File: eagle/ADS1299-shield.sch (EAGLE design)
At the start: 133 parts, among them IC1 ADS1299IPAG, IC2 TPS72325DBVT, IC3 TPS73225DBVT, IC5 24AA256UID, IC6 TPS604XXDBV, IC7 OPA376DBV, IC8 OPA376DBV, IC9 TXS0102DCTR, J16 EXTERNAL_SYNC, J8 Electrode Connector, U2 TXB0108PWR, U3 TXB0108PWR

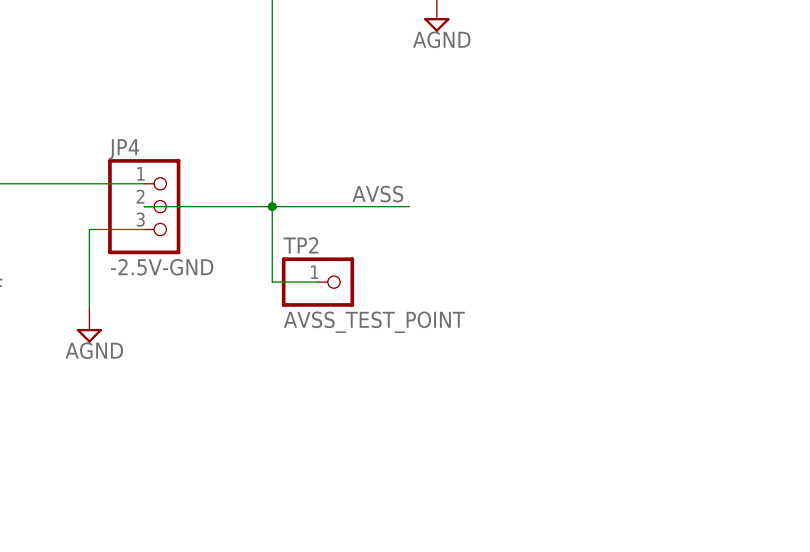
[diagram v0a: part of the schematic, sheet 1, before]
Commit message: fixed problem with test point 2
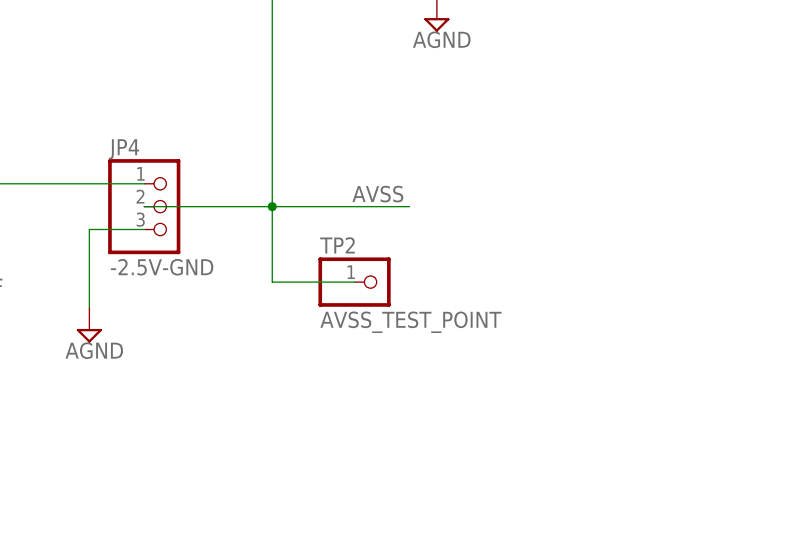
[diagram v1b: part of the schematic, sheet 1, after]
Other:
- moved on the sheet: TP2
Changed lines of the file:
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@@
 <part name="SPI" library="SmartPrj" deviceset="PINHD-2X3" device="" value="SPI"/>
 <part name="TP1" library="adafruit" deviceset="PINHD-1X1" device="" value="AVDD_TEST_POINT"/>
-<part name="TP2" library="adafruit" deviceset="PINHD-1X1" device="" value="AVSS_TEST_POINT"/>
 <part name="U$5" library="adafruit" deviceset="FIDUCIAL" device=""/>
 <part name="U$6" library="adafruit" deviceset="FIDUCIAL" device=""/>
@@
 <part name="TP3" library="adafruit" deviceset="PINHD-1X1" device="" value="AGND_TEST_POINT"/>
 <part name="SUPPLY55" library="supply2" deviceset="AGND" device=""/>
+<part name="TP2" library="adafruit" deviceset="PINHD-1X1" device="" value="AVSS_TEST_POINT"/>
 </parts>
 <sheets>
@@
 <instance part="D1" gate="G$1" x="272.034" y="43.18" rot="R90"/>
 <instance part="TP1" gate="G$1" x="184.912" y="113.792"/>
-<instance part="TP2" gate="G$1" x="184.15" y="33.782"/>
 <instance part="TP3" gate="G$1" x="212.852" y="73.152"/>
 <instance part="SUPPLY55" gate="G$1" x="194.818" y="62.992"/>
+<instance part="TP2" gate="G$1" x="188.214" y="33.782"/>
 </instances>
 <busses>
@@
 <pinref part="JP4" gate="A" pin="2"/>
 <wire x1="162.306" y1="42.164" x2="176.53" y2="42.164" width="0.1524" layer="91"/>
+<wire x1="185.674" y1="33.782" x2="176.53" y2="33.782" width="0.1524" layer="91"/>
+<wire x1="176.53" y1="33.782" x2="176.53" y2="42.164" width="0.1524" layer="91"/>
 <pinref part="TP2" gate="G$1" pin="1"/>
-<wire x1="181.61" y1="33.782" x2="176.53" y2="33.782" width="0.1524" layer="91"/>
-<wire x1="176.53" y1="33.782" x2="176.53" y2="42.164" width="0.1524" layer="91"/>
-</segment>
-<segment>
+</segment>
+<segment>

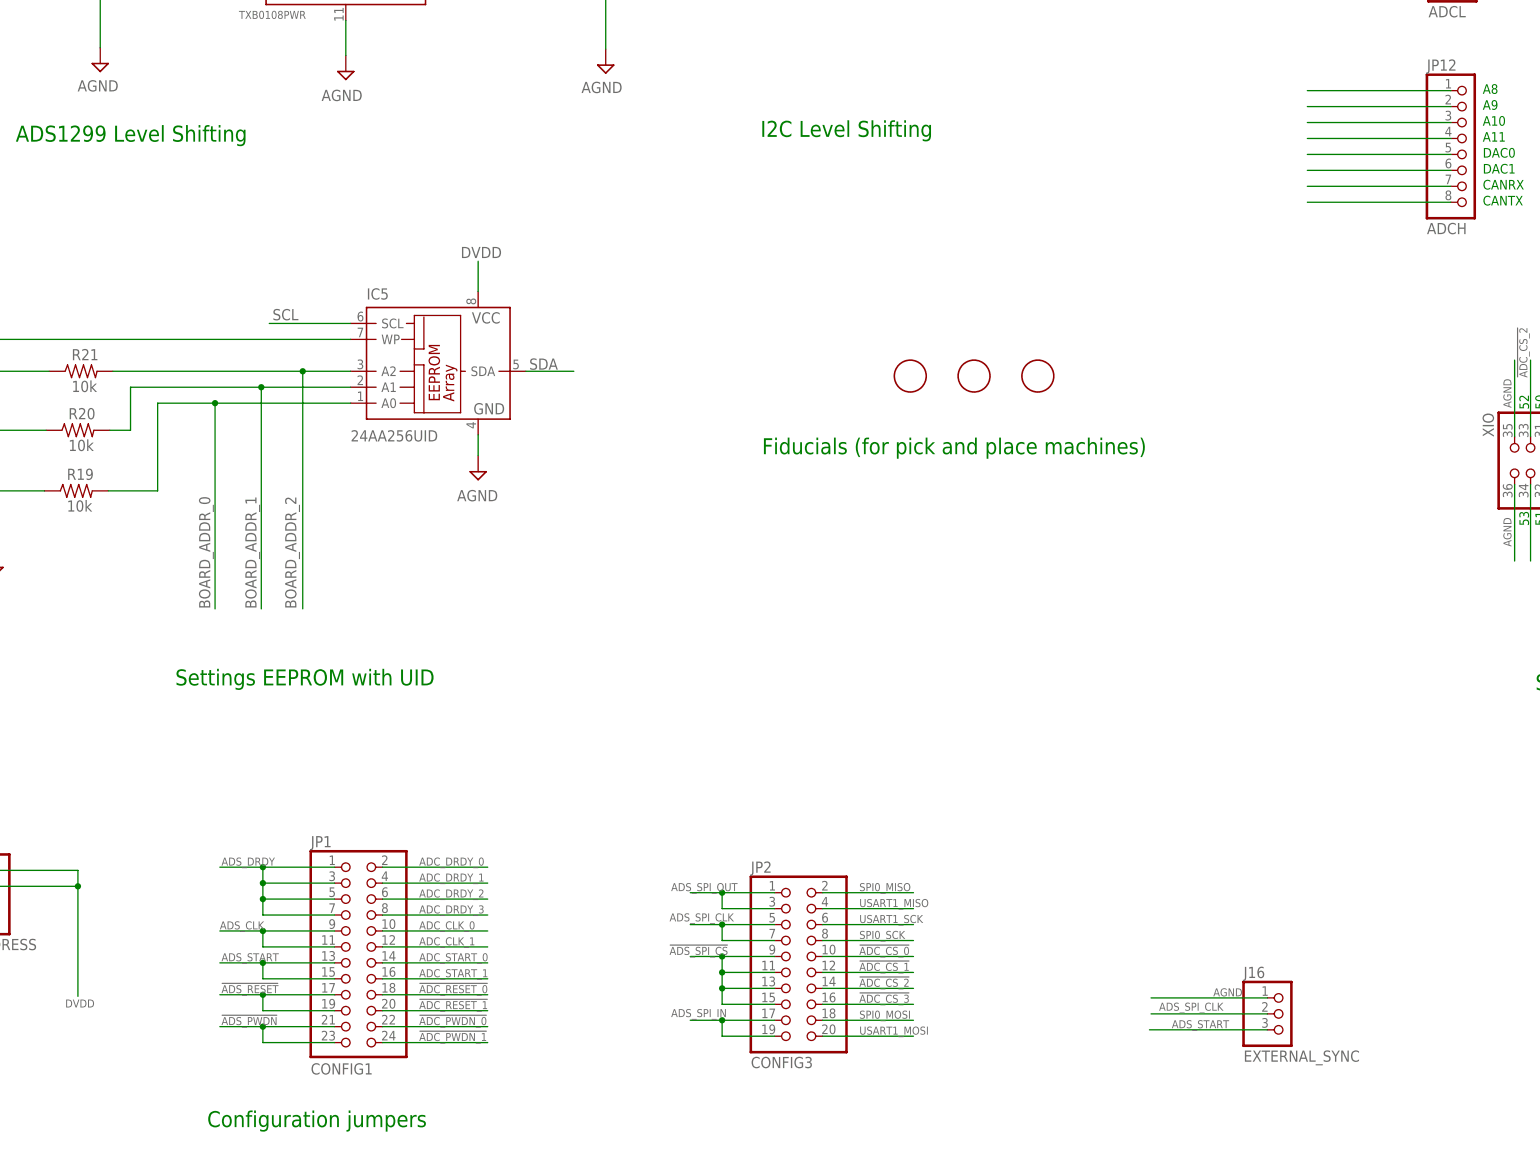
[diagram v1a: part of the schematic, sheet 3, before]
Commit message: minor clearance and legend improvements
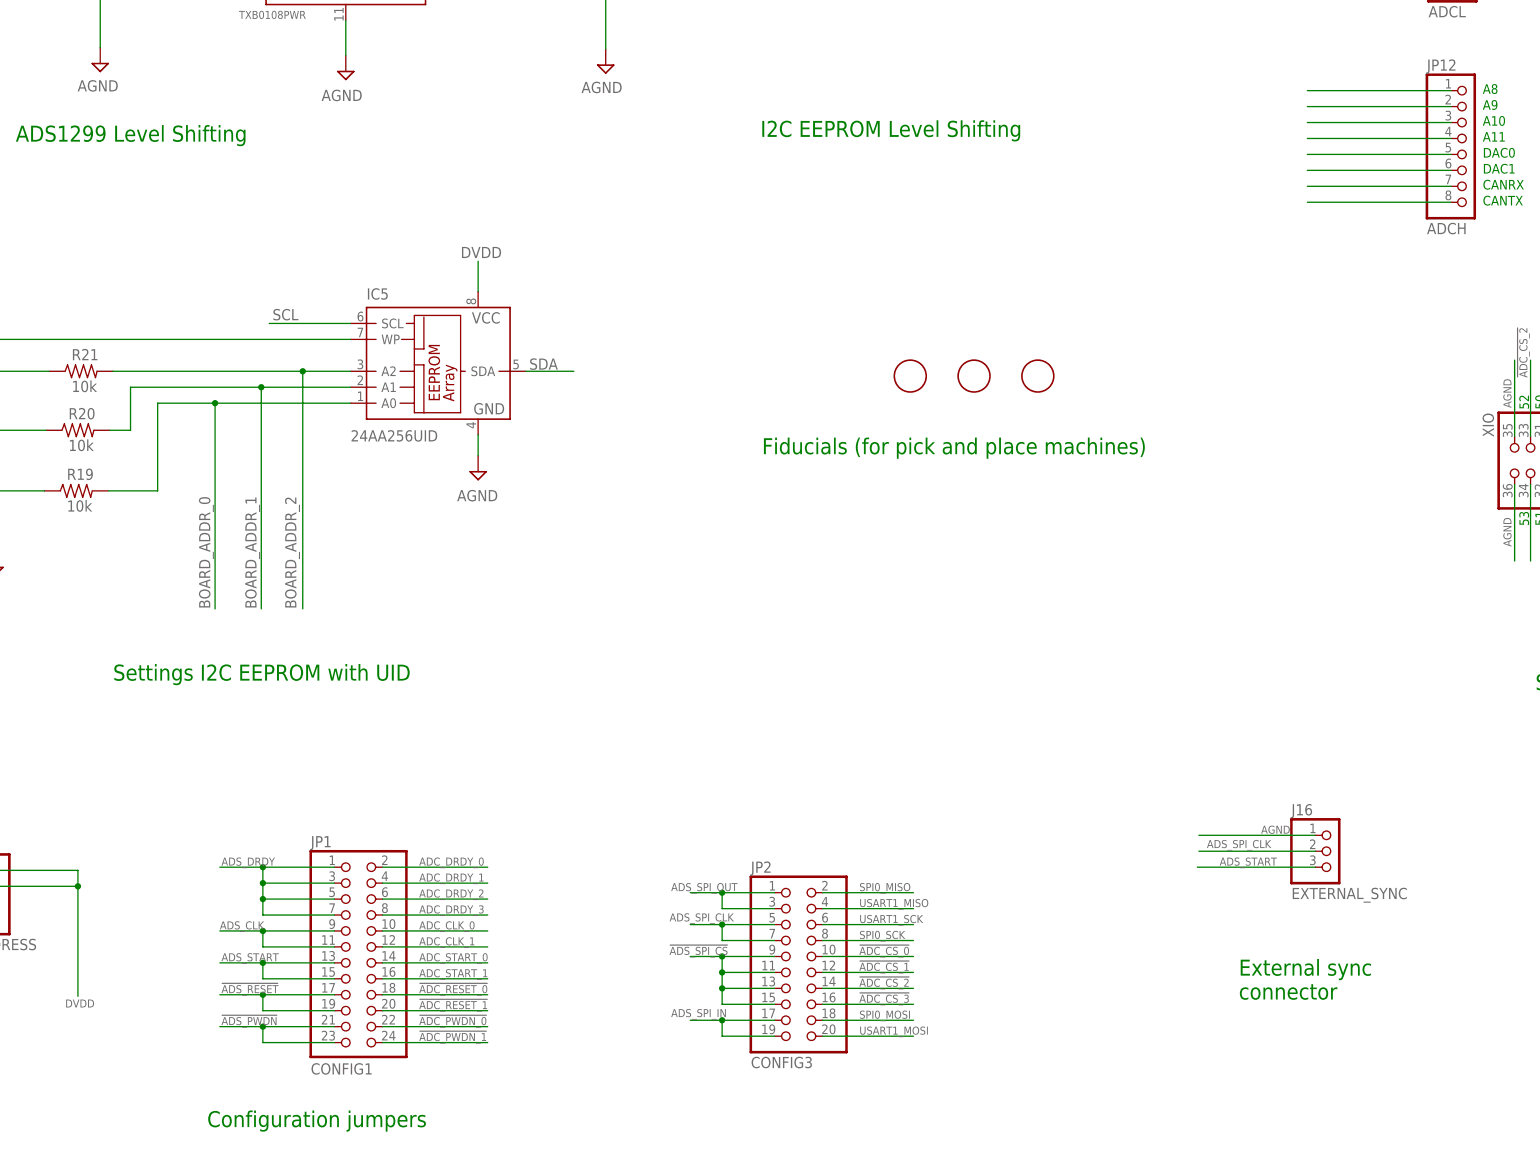
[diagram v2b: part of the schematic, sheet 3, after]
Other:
- note added: "External sync connector"
- note added: "I2C EEPROM Level Shifting"
- note added: "Settings I2C EEPROM with UID"
- note removed: "I2C Level Shifting"
- note removed: "Settings EEPROM with UID"
- moved on the sheet: J16
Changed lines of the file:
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@@
 <text x="103.886" y="14.986" size="2.54" layer="91">Configuration jumpers</text>
 <text x="73.406" y="171.958" size="2.54" layer="91">ADS1299 Level Shifting</text>
-<text x="98.806" y="85.344" size="2.54" layer="91">Settings EEPROM with UID</text>
+<text x="88.9" y="86.106" size="2.54" layer="91">Settings I2C EEPROM with UID</text>
 <text x="38.354" y="44.958" size="1.27" layer="91">(2 no-connect
 positions for
@@
 <text x="353.314" y="174.244" size="1.524" layer="91">TX2</text>
 <text x="353.314" y="171.704" size="1.524" layer="91">RX2</text>
-<text x="192.024" y="172.72" size="2.54" layer="91">I2C Level Shifting</text>
+<text x="192.024" y="172.72" size="2.54" layer="91">I2C EEPROM Level Shifting</text>
 <text x="304.8" y="264.16" size="1.778" layer="91">Pins not labeled are not connected (NC)</text>
+<text x="268.224" y="35.306" size="2.54" layer="91">External sync
+connector</text>
 </plain>
 <instances>
@@
 <attribute name="VALUE" x="16.383" y="180.721" size="1.778" layer="96" rot="R180"/>
 </instance>
-<instance part="J16" gate="G$1" x="275.336" y="33.02"/>
+<instance part="J16" gate="G$1" x="282.956" y="58.928"/>
 <instance part="JP2" gate="A" x="198.12" y="40.894"/>
 <instance part="R2" gate="G$1" x="25.908" y="226.822" smashed="yes">
@@
 </segment>
 <segment>
-<wire x1="272.796" y1="35.56" x2="254.254" y2="35.56" width="0.1524" layer="91"/>
-<label x="264.16" y="35.814" size="1.27" layer="95"/>
+<wire x1="280.416" y1="61.468" x2="261.874" y2="61.468" width="0.1524" layer="91"/>
+<label x="271.78" y="61.722" size="1.27" layer="95"/>
 <pinref part="J16" gate="G$1" pin="1"/>
 </segment>
@@
 </segment>
 <segment>
-<wire x1="272.796" y1="33.02" x2="254.254" y2="33.02" width="0.1524" layer="91"/>
-<label x="255.524" y="33.528" size="1.27" layer="95"/>
+<wire x1="280.416" y1="58.928" x2="261.874" y2="58.928" width="0.1524" layer="91"/>
+<label x="263.144" y="59.436" size="1.27" layer="95"/>
 <pinref part="J16" gate="G$1" pin="2"/>
 </segment>
@@
 <segment>
 <pinref part="J16" gate="G$1" pin="3"/>
-<wire x1="272.796" y1="30.48" x2="254" y2="30.48" width="0.1524" layer="91"/>
-<label x="257.556" y="30.734" size="1.27" layer="95"/>
-</segment>
-</net>
+<wire x1="280.416" y1="56.388" x2="261.62" y2="56.388" width="0.1524" layer="91"/>
+<label x="265.176" y="56.642" size="1.27" layer="95"/>
+</segment>
+</net>

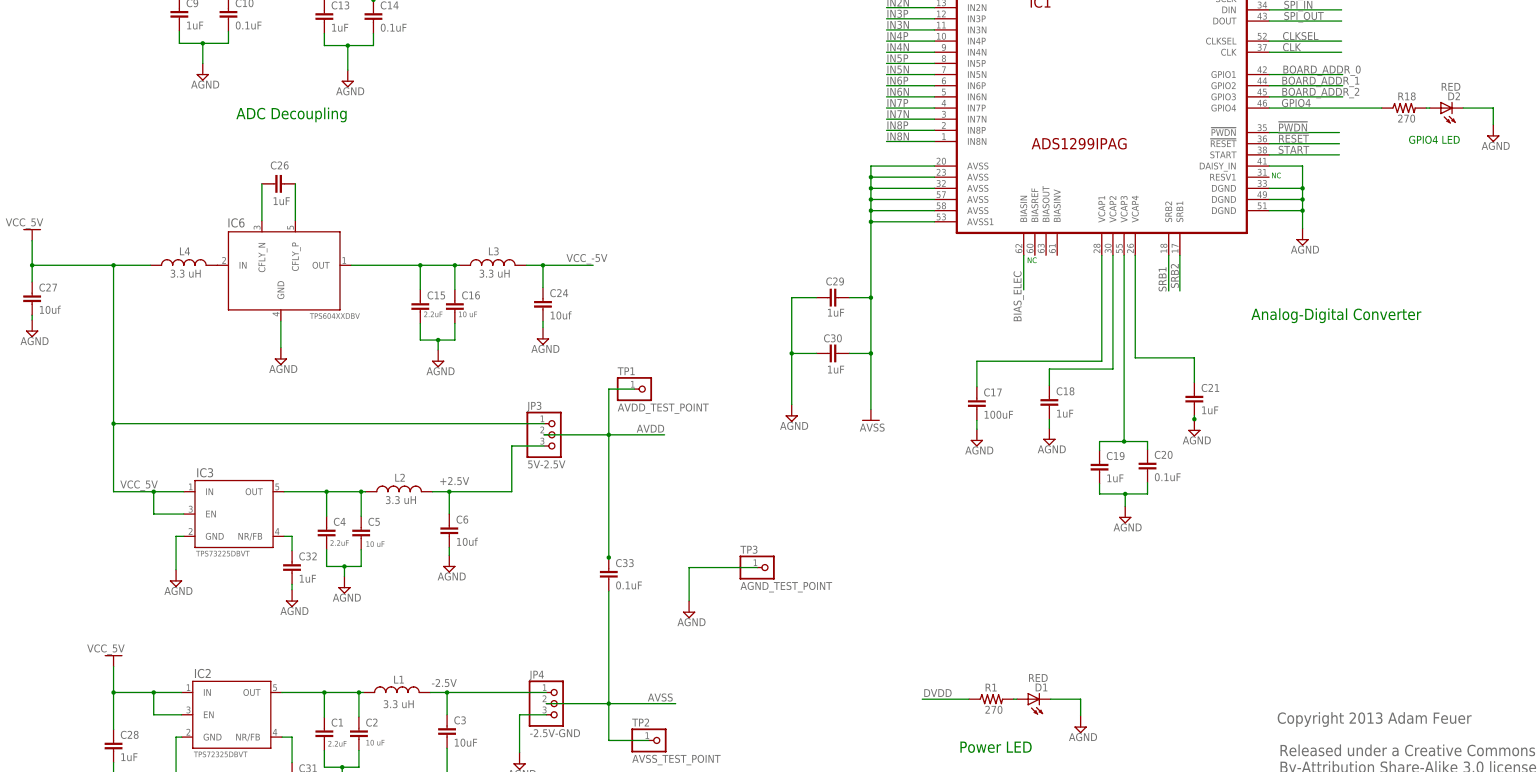
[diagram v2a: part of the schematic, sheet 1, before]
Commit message: widened many power traces; improved AVDD and AVSS routing
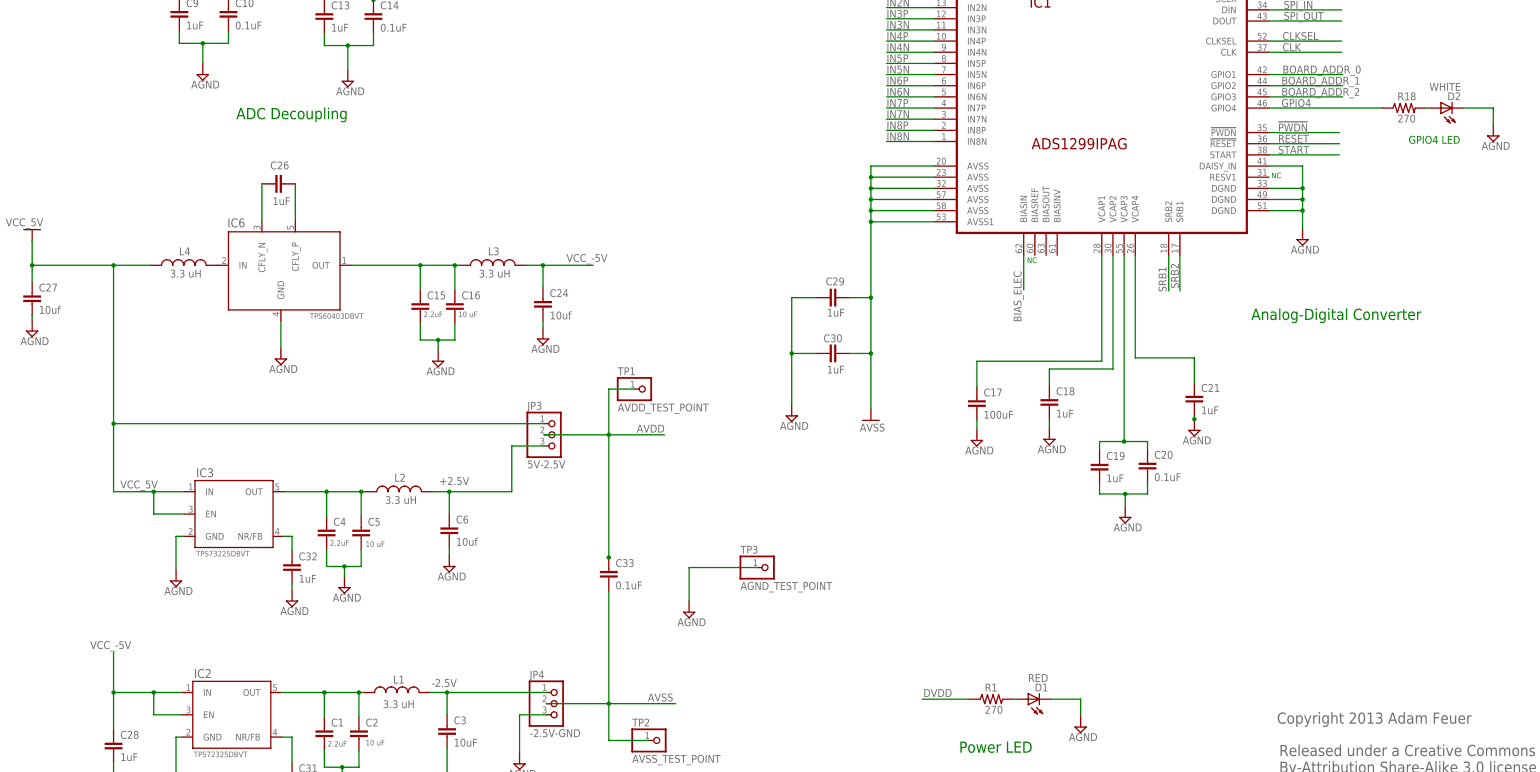
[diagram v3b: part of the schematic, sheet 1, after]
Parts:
- C17: device SparkFun-Passives:CAP0603-CAP -> SparkFun-Passives:CAP1210
- D2: value RED -> WHITE; device SparkFun-LED:LED-RED1206 -> SparkFun-LED:LED-WHITE
- IC6: value TPS604XXDBV -> TPS60403DBVT
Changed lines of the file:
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@@
 <part name="C13" library="SparkFun-Passives" deviceset="CAP" device="0603-CAP" value="1uF"/>
 <part name="C14" library="SparkFun-Passives" deviceset="CAP" device="0603-CAP" value="0.1uF"/>
-<part name="C17" library="SparkFun-Passives" deviceset="CAP" device="0603-CAP" value="100uF"/>
+<part name="C17" library="SparkFun-Passives" deviceset="CAP" device="1210" value="100uF"/>
 <part name="C18" library="SparkFun-Passives" deviceset="CAP" device="0603-CAP" value="1uF"/>
 <part name="C19" library="SparkFun-Passives" deviceset="CAP" device="0603-CAP" value="1uF"/>
@@
 <part name="SUPPLY9" library="supply2" deviceset="AGND" device=""/>
 <part name="SUPPLY11" library="supply2" deviceset="AGND" device=""/>
-<part name="IC6" library="TPS604xx" deviceset="TPS604XX" device="DBV"/>
+<part name="IC6" library="TPS604xx" deviceset="TPS604XX" device="DBV" value="TPS60403DBVT"/>
 <part name="C26" library="SparkFun-Passives" deviceset="CAP" device="0603-CAP" value="1uF"/>
 <part name="L4" library="SparkFun-Passives" deviceset="INDUCTOR" device="0603" value="3.3 uH"/>
@@
 <part name="SUPPLY19" library="supply2" deviceset="AGND" device=""/>
 <part name="SUPPLY23" library="supply2" deviceset="AGND" device=""/>
-<part name="VCC_5V1" library="SparkFun-Aesthetics" deviceset="GND" device="" value="VCC_5V"/>
 <part name="SUPPLY25" library="supply2" deviceset="AGND" device=""/>
 <part name="C33" library="SparkFun-Passives" deviceset="CAP" device="0603-CAP" value="0.1uF"/>
@@
 <part name="R18" library="SparkFun-Passives" deviceset="RESISTOR" device="0603-RES" value="270"/>
 <part name="SUPPLY40" library="supply2" deviceset="AGND" device=""/>
-<part name="D2" library="SparkFun-LED" deviceset="LED-RED" device="1206" value="RED"/>
+<part name="D2" library="SparkFun-LED" deviceset="LED-WHITE" device="" value="WHITE"/>
 <part name="IC5" library="microchip" deviceset="24*" device="SN" technology="LC256" value="24AA256UID"/>
 <part name="R19" library="SparkFun-Passives" deviceset="RESISTOR" device="0603-RES" value="10k"/>
@@
 <instance part="SUPPLY19" gate="G$1" x="104.394" y="17.272"/>
 <instance part="SUPPLY23" gate="G$1" x="104.394" y="65.532"/>
-<instance part="VCC_5V1" gate="1" x="63.754" y="53.086" smashed="yes" rot="R180">
-<attribute name="VALUE" x="66.294" y="55.626" size="1.778" layer="96" rot="R180"/>
-</instance>
 <instance part="SUPPLY25" gate="G$1" x="156.21" y="28.448"/>
 <instance part="C33" gate="G$1" x="176.53" y="70.358"/>
@@
 <wire x1="63.754" y1="44.704" x2="63.754" y2="36.322" width="0.1524" layer="91"/>
 <pinref part="C28" gate="G$1" pin="1"/>
-<pinref part="VCC_5V1" gate="1" pin="GND"/>
-<wire x1="63.754" y1="50.546" x2="63.754" y2="44.704" width="0.1524" layer="91"/>
+<wire x1="63.754" y1="53.848" x2="63.754" y2="44.704" width="0.1524" layer="91"/>
 <junction x="63.754" y="44.704"/>
-</segment>
-</net>
+<label x="58.42" y="54.61" size="1.778" layer="95"/>
+</segment>
+</net>
